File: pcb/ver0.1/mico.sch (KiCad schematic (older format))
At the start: 55 parts, among them J1 USB_A, J2 SWD Prog, U1 MCP1702, U2 MP23DB01HPTR, U3 W25Q128JV, U4 RP2040, U5 MP23DB01HPTR, U6 MP23DB01HPTR, U7 MP23DB01HPTR, Y1 H130B-12.000-20-3050-EXT-TR

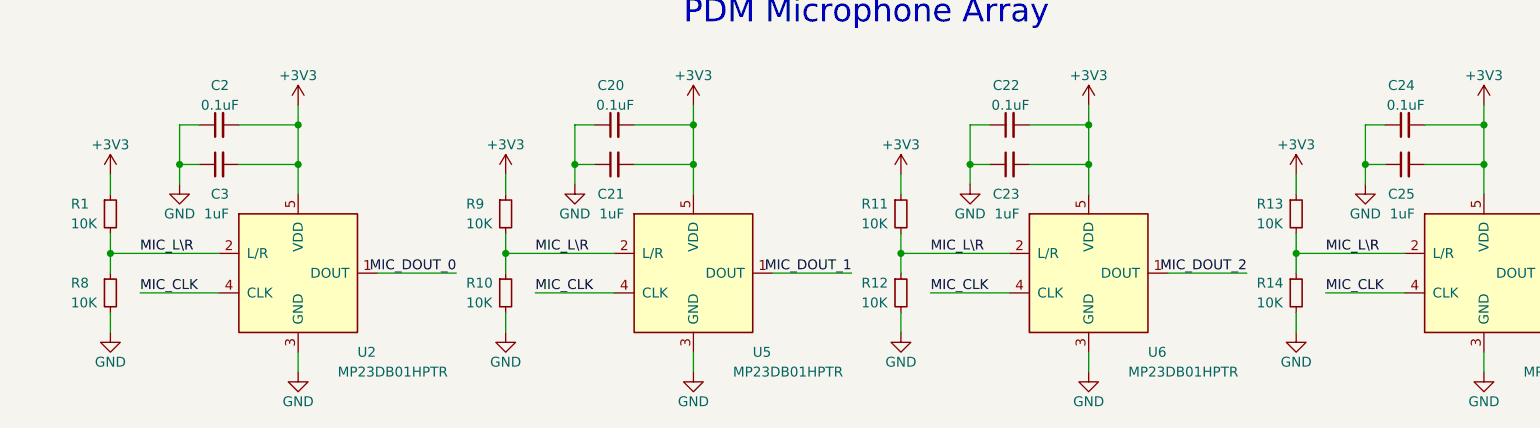
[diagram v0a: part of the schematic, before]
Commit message: wire up mics, just need to connect data lines
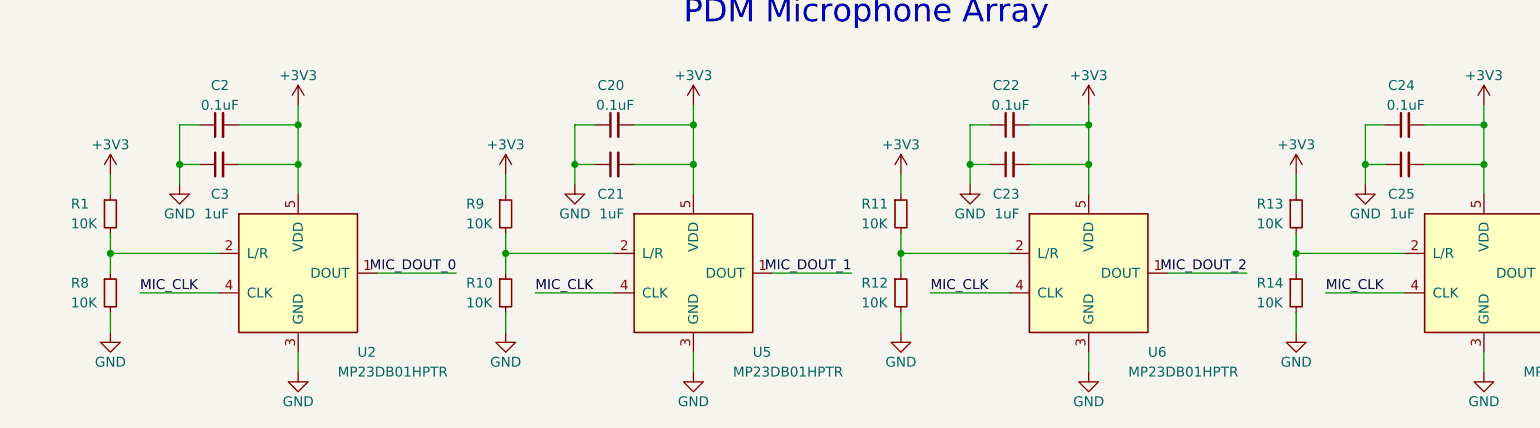
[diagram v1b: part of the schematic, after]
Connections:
- removed net MIC_L\R: R1.2, R10.1, R11.2, R12.1, R13.2, R14.1, R8.1, R9.2, U2.2 (L/R), U5.2 (L/R), U6.2 (L/R), U7.2 (L/R)
- new net: R1.2, R8.1, U2.2 (L/R)
- new net: R10.1, R9.2, U5.2 (L/R)
- new net: R11.2, R12.1, U6.2 (L/R)
- new net: R13.2, R14.1, U7.2 (L/R)
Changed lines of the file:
@@
 Wire Wire Line
 	4450 11750 4050 11750
-Text Label 4050 11550 0    50   ~ 0
-MIC_L\R
 $Comp
 L power:+3V3 #PWR09
@@
 Wire Wire Line
 	6450 11750 6050 11750
-Text Label 6050 11550 0    50   ~ 0
-MIC_L\R
 $Comp
 L power:+3V3 #PWR035
@@
 Wire Wire Line
 	8450 11750 8050 11750
-Text Label 8050 11550 0    50   ~ 0
-MIC_L\R
 $Comp
 L power:+3V3 #PWR040
@@
 Wire Wire Line
 	10450 11750 10050 11750
-Text Label 10050 11550 0    50   ~ 0
-MIC_L\R
 $Comp
 L power:+3V3 #PWR045

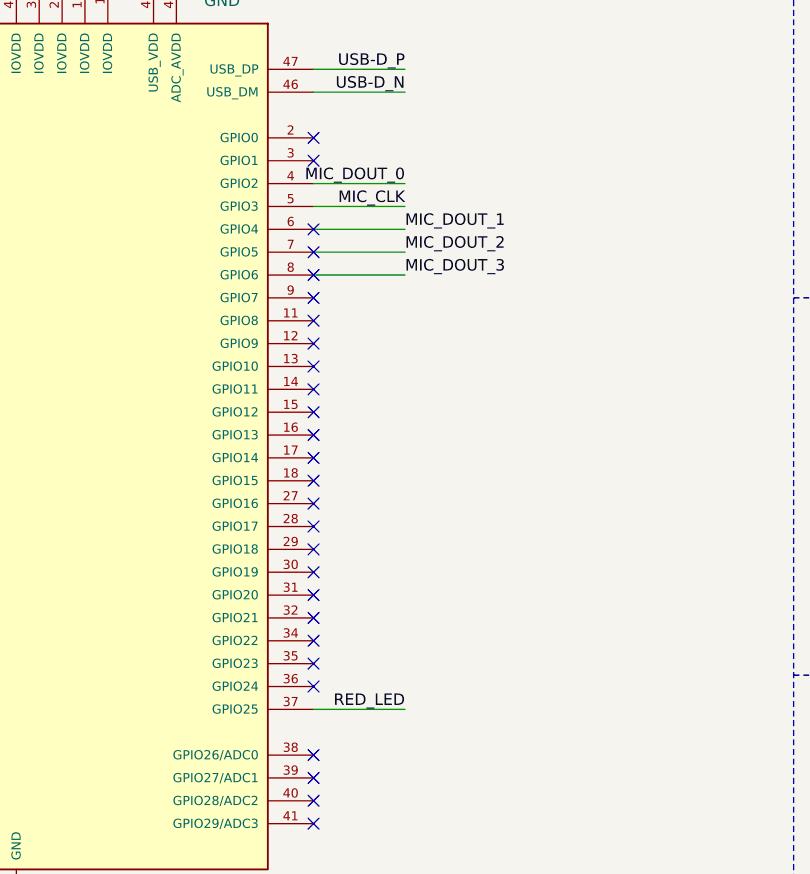
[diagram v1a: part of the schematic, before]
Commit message: completed pcb layout
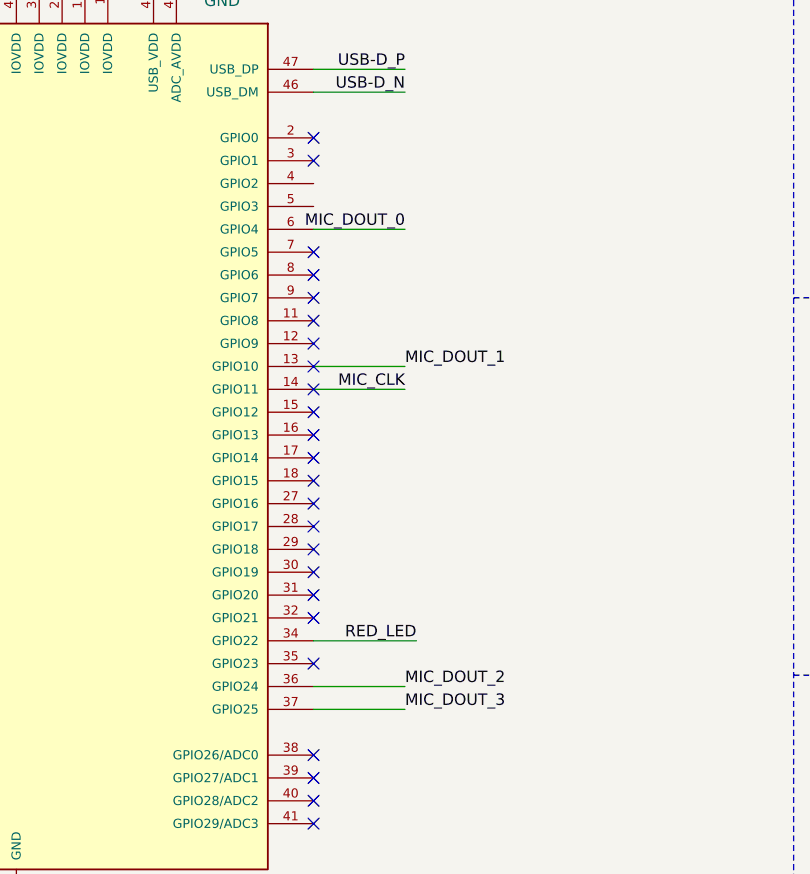
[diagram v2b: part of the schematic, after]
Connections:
- net MIC_CLK: now also U4.14 (GPIO11); no longer U4.5 (GPIO3)
- net MIC_DOUT_0: now also U4.6 (GPIO4); no longer U4.4 (GPIO2)
- net MIC_DOUT_1: now also U4.13 (GPIO10); no longer U4.6 (GPIO4)
- net MIC_DOUT_2: now also U4.36 (GPIO24); no longer U4.7 (GPIO5)
- net MIC_DOUT_3: now also U4.37 (GPIO25); no longer U4.8 (GPIO6)
- net RED_LED: now also U4.34 (GPIO22); no longer U4.37 (GPIO25)
- no-connect marks 27 -> 24
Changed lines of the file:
@@
 	1    0    0    -1
 $EndComp
-Wire Wire Line
-	5500 6450 5500 6550
-Wire Wire Line
-	5900 6450 5900 6550
 $Comp
 L power:GND #PWR021
@@
 Wire Wire Line
 	8850 1550 8850 1450
-Text Label 7600 3350 2    50   ~ 0
+Text Label 7600 4150 2    50   ~ 0
 MIC_CLK
 $Comp
@@
 Wire Wire Line
 	9600 1550 9950 1550
-Text Label 7600 5550 2    50   ~ 0
-RED_LED
-Wire Wire Line
-	7200 5550 7600 5550
 Text Label 9600 1550 0    50   ~ 0
 RED_LED
@@
 	1    4250 4950
 	0    -1   -1   0
-$EndComp
-$Comp
-L mico:RP2040 U4
-U 1 1 6199EEDE
-P 5900 4450
-F 0 "U4" H 6450 2550 50  0000 C CNN
-F 1 "RP2040" H 6450 2450 50  0000 C CNN
-F 2 "mico:QFN40P700X700X90-57N" H 5400 4450 50  0001 L BNN
-F 3 "" H 5700 4450 50  0001 L BNN
-F 4 "0.9 mm" H 5700 4450 50  0001 L BNN "MAXIMUM_PACKAGE_HEIGHT"
-F 5 "Raspberry Pi" H 5400 4450 50  0001 L BNN "MANUFACTURER"
-F 6 "1.6.1" H 5700 4450 50  0001 L BNN "PARTREV"
-F 7 "IPC 7351B" H 5400 4450 50  0001 L BNN "STANDARD"
-	1    5900 4450
-	1    0    0    -1
 $EndComp
 $Comp
@@
 Text Notes 5350 900  0    118  ~ 0
 RP2040
-Wire Wire Line
-	7200 3350 7600 3350
-Wire Wire Line
-	7200 3250 7600 3250
 $Comp
 L Device:Crystal_GND24_Small Y1
@@
 Wire Wire Line
 	2050 1400 1500 1400
-Wire Wire Line
-	7200 2750 7600 2750
-Wire Wire Line
-	7600 2850 7200 2850
 $Comp
 L mico-rescue:USB_A-Connector J1
@@
 NoConn ~ 7200 5850
 NoConn ~ 7200 5750
-NoConn ~ 7200 5450
 NoConn ~ 7200 5350
-NoConn ~ 7200 5250
 NoConn ~ 7200 5150
 NoConn ~ 7200 5050
@@
 NoConn ~ 7200 3650
 NoConn ~ 7200 3550
-NoConn ~ 7200 3450
 NoConn ~ 7200 3150
 NoConn ~ 7200 3050
@@
 Text Label 4050 11750 0    50   ~ 0
 MIC_CLK
-Text Label 7600 3250 2    50   ~ 0
+Text Label 7600 3450 2    50   ~ 0
 MIC_DOUT_0
 Wire Wire Line
@@
 Text Label 10050 11750 0    50   ~ 0
 MIC_CLK
-Wire Wire Line
-	7200 3450 7600 3450
-Wire Wire Line
-	7200 3550 7600 3550
-Wire Wire Line
-	7200 3650 7600 3650
-Text Label 7600 3450 0    50   ~ 0
+Text Label 7600 4050 0    50   ~ 0
 MIC_DOUT_1
-Text Label 7600 3550 0    50   ~ 0
-MIC_DOUT_2
-Text Label 7600 3650 0    50   ~ 0
-MIC_DOUT_3
 Text Label 5650 11650 2    50   ~ 0
 MIC_DOUT_0
@@
 	1    0    0    -1
 $EndComp
+Wire Wire Line
+	7200 4050 7600 4050
+Wire Wire Line
+	7200 4150 7600 4150
+Wire Wire Line
+	7200 3450 7600 3450
+Wire Wire Line
+	7600 2850 7200 2850
+Wire Wire Line
+	7200 2750 7600 2750
+Wire Wire Line
+	5900 6450 5900 6550
+Wire Wire Line
+	5500 6450 5500 6550
+$Comp
+L mico:RP2040 U4
+U 1 1 6199EEDE
+P 5900 4450
+F 0 "U4" H 6450 2550 50  0000 C CNN
+F 1 "RP2040" H 6450 2450 50  0000 C CNN
+F 2 "mico:QFN40P700X700X90-57N" H 5400 4450 50  0001 L BNN
+F 3 "" H 5700 4450 50  0001 L BNN
+F 4 "0.9 mm" H 5700 4450 50  0001 L BNN "MAXIMUM_PACKAGE_HEIGHT"
+F 5 "Raspberry Pi" H 5400 4450 50  0001 L BNN "MANUFACTURER"
+F 6 "1.6.1" H 5700 4450 50  0001 L BNN "PARTREV"
+F 7 "IPC 7351B" H 5400 4450 50  0001 L BNN "STANDARD"
+	1    5900 4450
+	1    0    0    -1
+$EndComp
+Wire Wire Line
+	7200 5550 7600 5550
+Text Label 7600 5550 0    50   ~ 0
+MIC_DOUT_3
+Text Label 7600 5450 0    50   ~ 0
+MIC_DOUT_2
+Wire Wire Line
+	7200 5450 7600 5450
+Text Label 7650 5250 2    50   ~ 0
+RED_LED
+Wire Wire Line
+	7650 5250 7200 5250
 $EndSCHEMATC
